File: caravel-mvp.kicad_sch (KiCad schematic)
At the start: 46 parts, among them J2 Conn_01x02, J3 Conn_02x04_Odd_Even, J4 Conn_01x06, J6 Conn_02x18_Odd_Even, J6 USB_C_Receptacle_USB2.0, J9 613012243121, SW3 B3U-1000P, U1 Caravel_QFN, U1 W25Q32JVSS, X1 10MHz

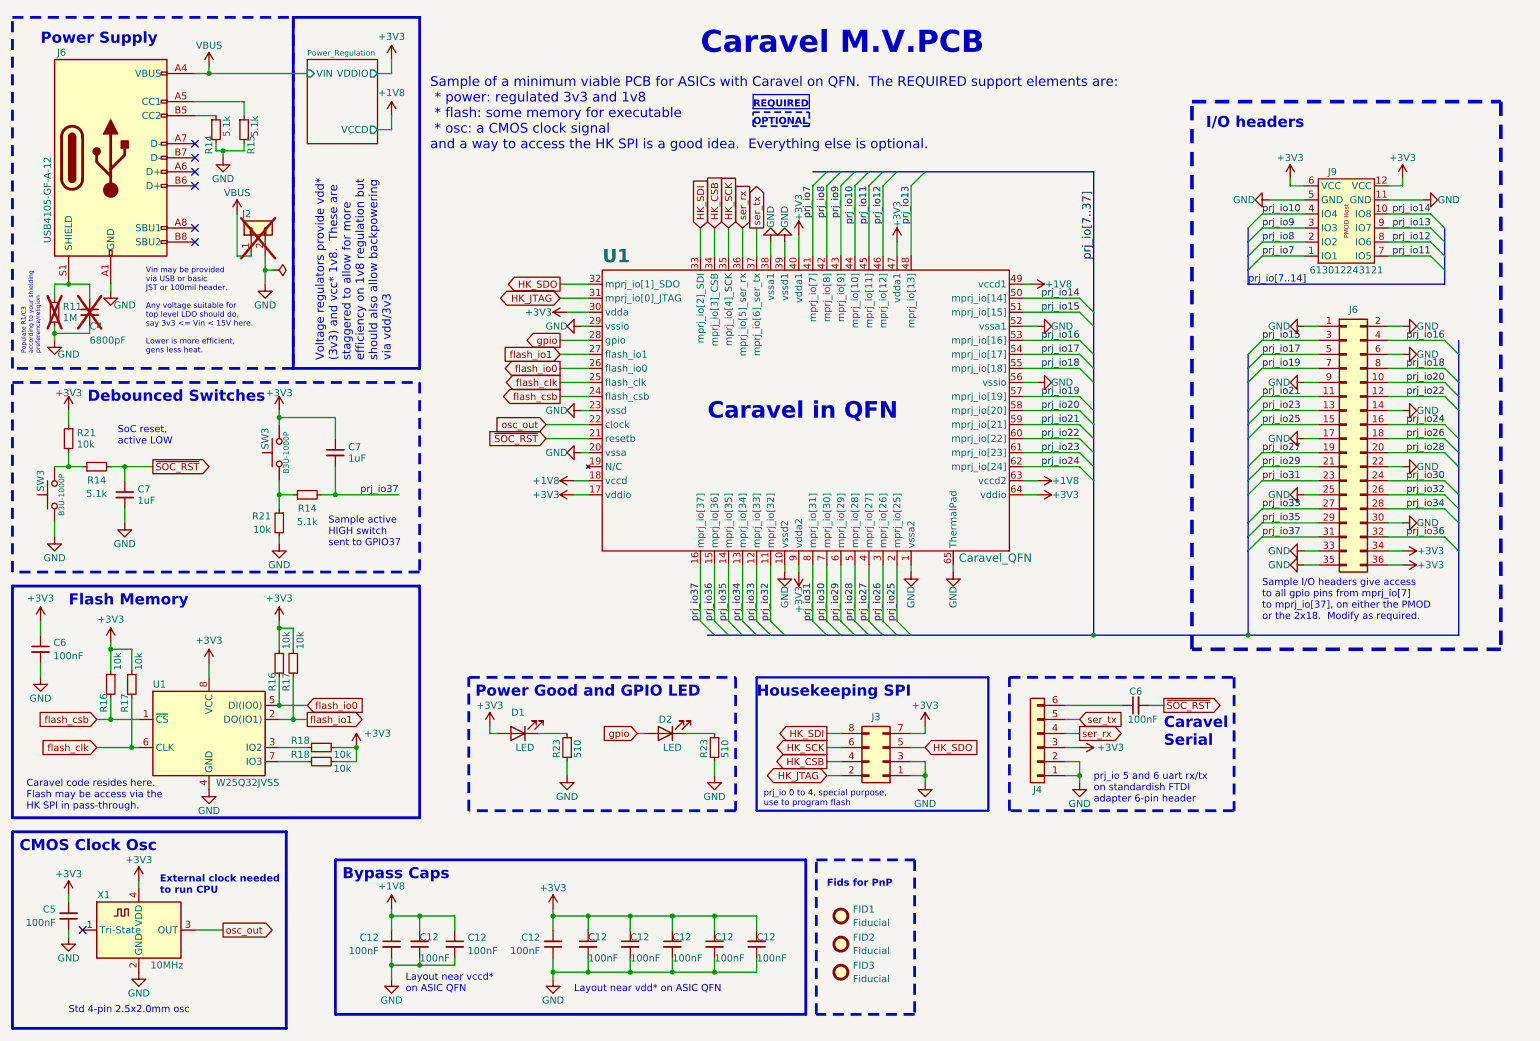
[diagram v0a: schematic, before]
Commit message: TinyTapeout 1-2-3 version
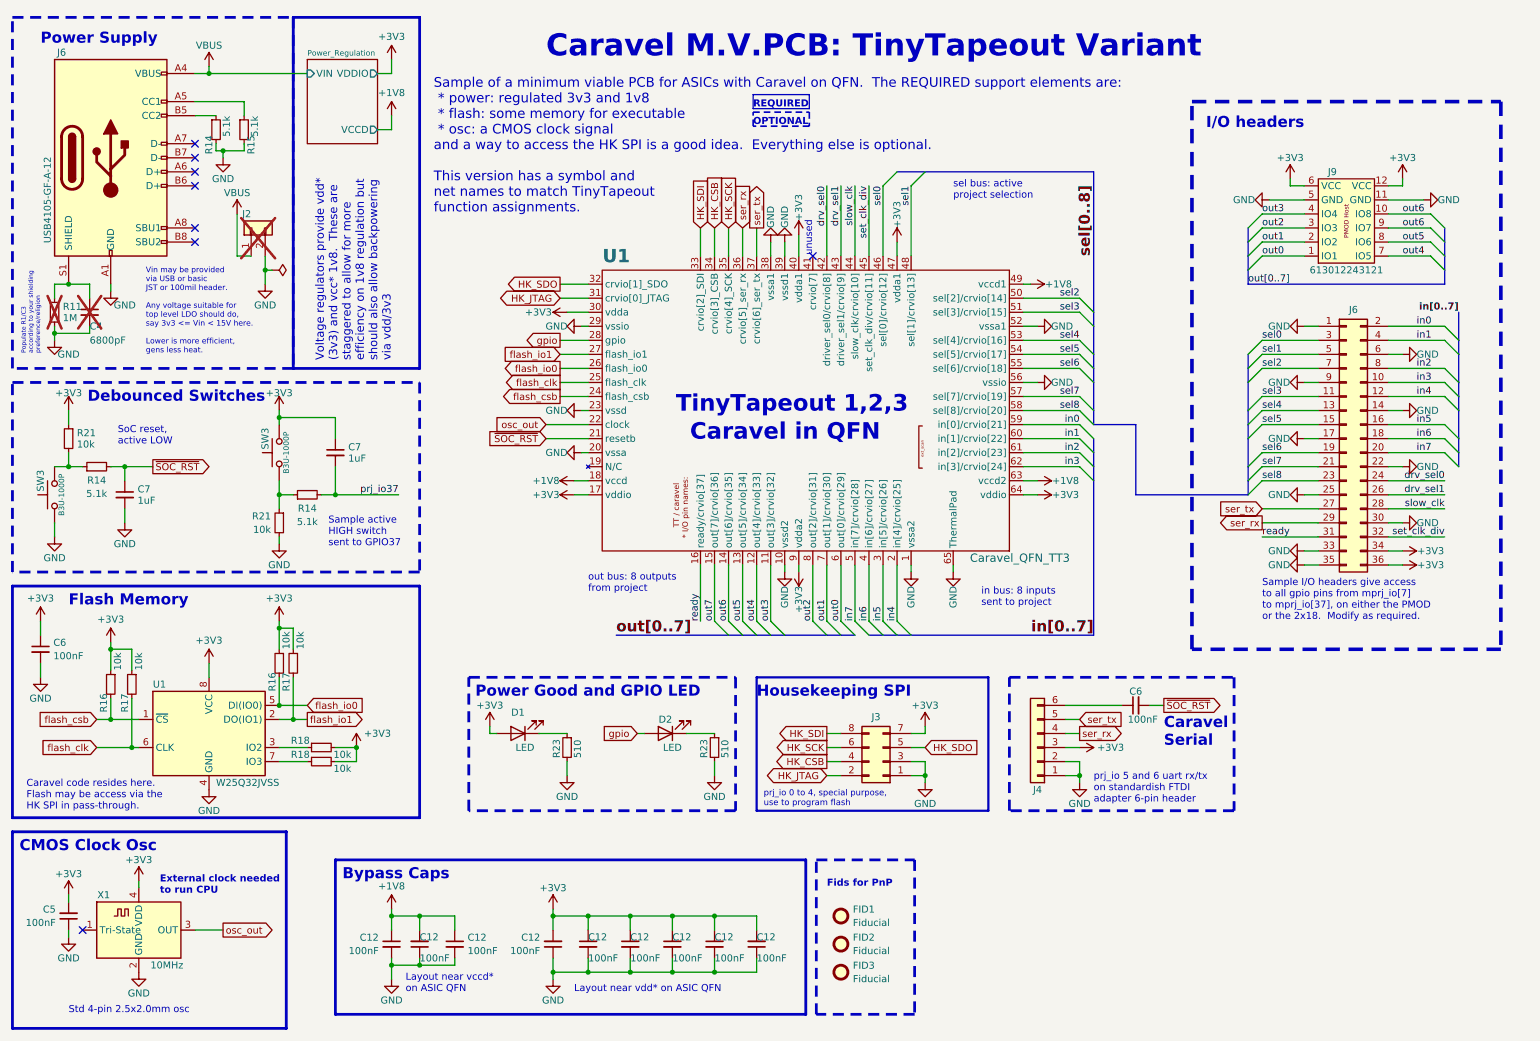
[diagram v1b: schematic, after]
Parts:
- U1: value Caravel_QFN -> Caravel_QFN_TT3; symbol TinyTapeout:Caravel_QFN -> TinyTapeout:Caravel_QFN_TT3
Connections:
- net GND: no longer J6.2 (Pin_2)
- net prj_io37: no longer J6.31 (Pin_31), U1.16 (mprj_io[37])
- net ser_rx: now also J6.29 (Pin_29)
- net ser_tx: now also J6.27 (Pin_27)
- net prj_io10 renamed out3
- net out3: now also U1.11 (out[3]/crvio[32]); no longer U1.44 (mprj_io[10])
- net prj_io11 renamed out4
- net out4: now also U1.12 (out[4]/crvio[33]); no longer U1.45 (mprj_io[11])
- net prj_io12 renamed out5
- net out5: now also U1.13 (out[5]/crvio[34]); no longer U1.46 (mprj_io[12])
- net prj_io13 renamed out6
- net out6: now also J9.10 (IO8), U1.14 (out[6]/crvio[35]); no longer U1.48 (mprj_io[13])
- net prj_io14 renamed sel2
- net sel2: now also J6.7 (Pin_7); no longer J9.10 (IO8)
- net prj_io15 renamed sel0
- net sel0: now also U1.46 (sel[0]/crvio[12]); no longer U1.51 (mprj_io[15])
- net prj_io16 renamed in1
- net in1: now also U1.60 (in[1]/crvio[22]); no longer U1.53 (mprj_io[16])
- net prj_io17 renamed sel1
- net sel1: now also U1.48 (sel[1]/crvio[13]); no longer U1.54 (mprj_io[17])
- net prj_io18 renamed in2
- net in2: now also U1.61 (in[2]/crvio[23]); no longer U1.55 (mprj_io[18])
- net prj_io19 renamed sel7
- net sel7: now also J6.21 (Pin_21); no longer J6.7 (Pin_7)
- net prj_io20 renamed in3
- net in3: now also U1.62 (in[3]/crvio[24]); no longer U1.58 (mprj_io[20])
- net prj_io21 renamed in0
- net in0: now also J6.2 (Pin_2); no longer J6.11 (Pin_11)
- net prj_io22 renamed in4
- net in4: now also U1.2 (in[4]/crvio[25]); no longer U1.60 (mprj_io[22])
- net prj_io23 renamed sel4
- net sel4: now also U1.53 (sel[4]/crvio[16]); no longer U1.61 (mprj_io[23])
- net prj_io24 renamed in5
- net in5: now also U1.3 (in[5]/crvio[26]); no longer U1.62 (mprj_io[24])
- net prj_io25 renamed sel5
- net sel5: now also U1.54 (sel[5]/crvio[17]); no longer U1.2 (mprj_io[25])
- net prj_io26 renamed in6
- net in6: now also U1.4 (in[6]/crvio[27]); no longer U1.3 (mprj_io[26])
- net prj_io27 renamed sel6
- net sel6: now also U1.55 (sel[6]/crvio[18]); no longer U1.4 (mprj_io[27])
- net prj_io28 renamed in7
- net prj_io29 renamed out0
- net out0: now also J9.1 (IO1); no longer J6.21 (Pin_21)
- net prj_io30 renamed drv_sel0
- net drv_sel0: now also U1.42 (driver_sel0/crvio[8]); no longer U1.7 (mprj_io[30])
- net prj_io31 renamed out2
- net out2: now also J9.3 (IO3); no longer J6.23 (Pin_23)
- net prj_io32 renamed drv_sel1
- net drv_sel1: now also U1.43 (driver_sel1/crvio[9]); no longer U1.11 (mprj_io[32])
- removed net prj_io33: J6.27 (Pin_27), U1.12 (mprj_io[33])
- net prj_io34 renamed slow_clk
- net slow_clk: now also U1.44 (slow_clk/crvio[10]); no longer U1.13 (mprj_io[34])
- removed net prj_io35: J6.29 (Pin_29), U1.14 (mprj_io[35])
- net prj_io36 renamed out7
- net out7: no longer J6.32 (Pin_32)
- net prj_io7: no longer names the net of U1.41 (crvio[7])
- net prj_io7: no longer J9.1 (IO1)
- net prj_io8 renamed out1
- net out1: now also U1.7 (out[1]/crvio[30]); no longer U1.42 (mprj_io[8])
- removed net prj_io9: J9.3 (IO3), U1.43 (mprj_io[9])
- new net ready: J6.31 (Pin_31), U1.16 (ready/crvio[37])
- new net sel3: J6.11 (Pin_11), U1.51 (sel[3]/crvio[15])
- new net sel8: J6.23 (Pin_23), U1.58 (sel[8]/crvio[20])
- new net set_clk_div: J6.32 (Pin_32), U1.45 (set_clk_div/crvio[11])
- no-connect marks 7 -> 8
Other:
- note added: "Caravel M.V.PCB: TinyTapeout Variant"
- note added: "Sample of a minimum viable PCB for ASICs with Caravel on QFN. The REQUIRED support elements are: * power: regulated 3v3 and 1v8 * flash: some memory for executable * osc: a CMOS clock signal and a way to access the HK SPI is a good idea. Everything else is optional. This version has a symbol and net names to match TinyTapeout function assignments."
- note added: "TinyTapeout 1,2,3"
- note added: "in bus: 8 inputs sent to project"
- note added: "out bus: 8 outputs from project"
- note added: "sel bus: active project selection"
- note added: "unused"
- note removed: "Caravel M.V.PCB"
- note removed: "Sample of a minimum viable PCB for ASICs with Caravel on QFN. The REQUIRED support elements are: * power: regulated 3v3 and 1v8 * flash: some memory for executable * osc: a CMOS clock signal and a way to access the HK SPI is a good idea. Everything else is optional."
- title: Caravel Minimum Viable PCB Example -> Caravel Minimum Viable PCB Example: TinyTapeout Version

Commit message: TinyTapeout Stand-alone (no CPU) circuit and info
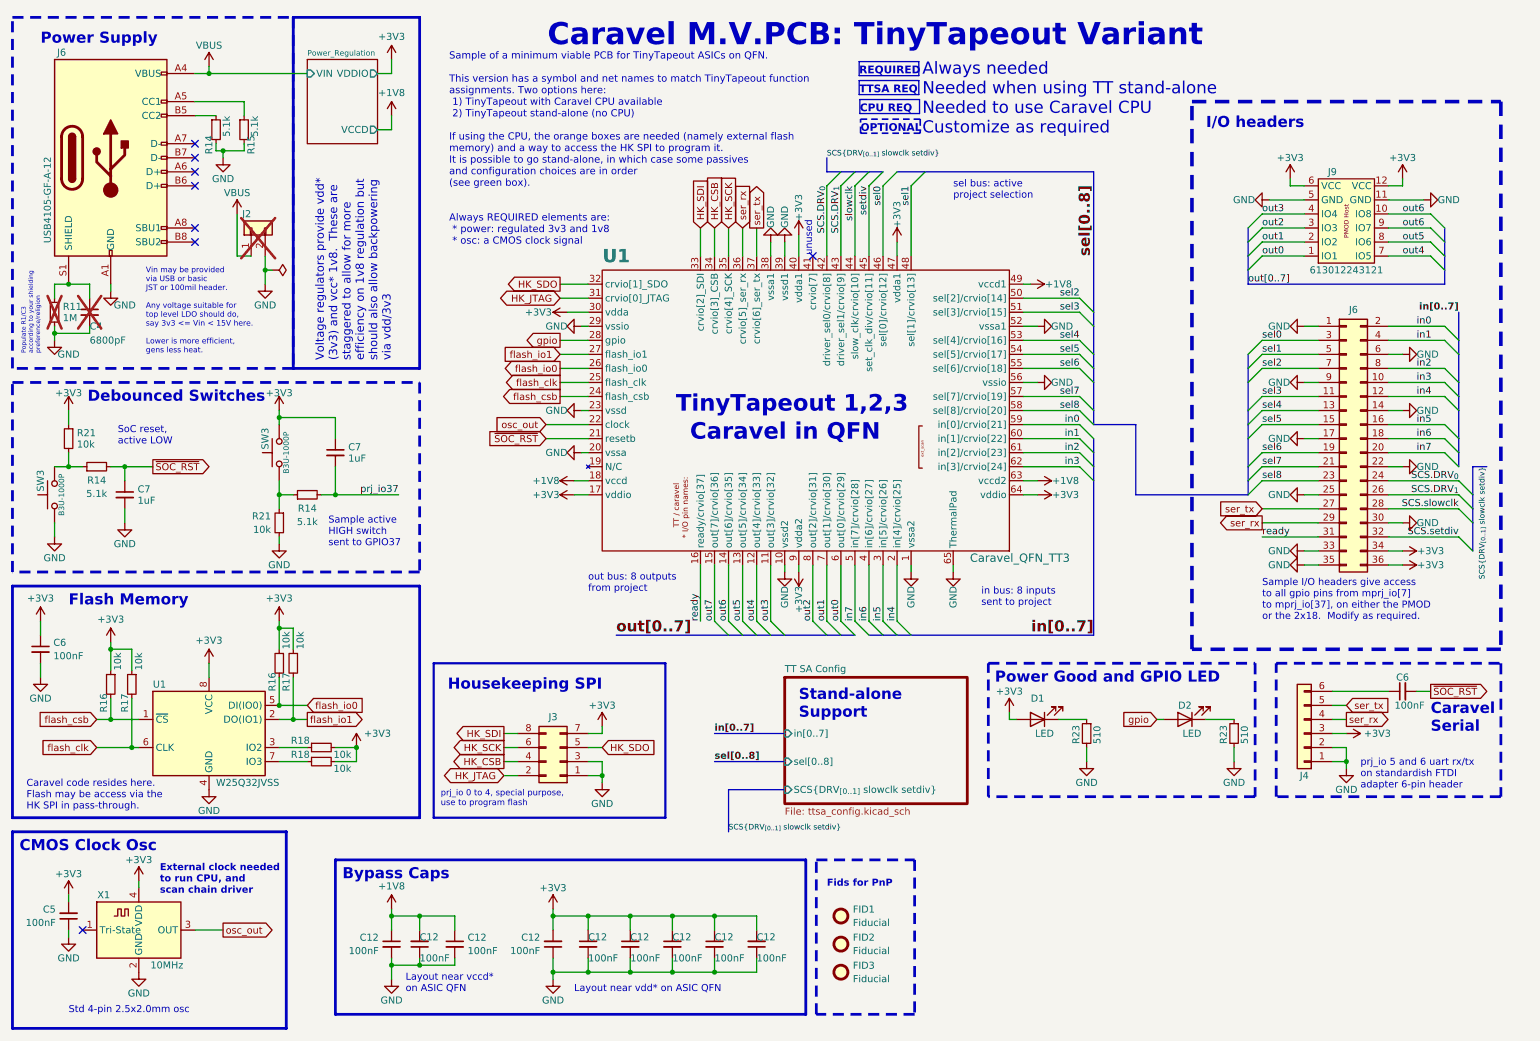
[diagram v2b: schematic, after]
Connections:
- net drv_sel0 renamed SCS.DRV_{0}
- net drv_sel1 renamed SCS.DRV_{1}
- net set_clk_div renamed SCS.setdiv
- net SCS.setdiv: no longer U1.45 (set_clk_div/crvio[11])
- net slow_clk renamed SCS.slowclk
- net SCS.slowclk: no longer U1.44 (slow_clk/crvio[10])
- new net setdiv: U1.45 (set_clk_div/crvio[11])
- new net slowclk: U1.44 (slow_clk/crvio[10])
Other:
- added sheet TT SA Config (ttsa_config.kicad_sch)
- note added: "Always needed Needed when using TT stand-alone Needed to use Caravel CPU Customize as required"
- note added: "CPU REQ"
- note added: "External clock needed to run CPU, and scan chain driver"
- note added: "Sample of a minimum viable PCB for TinyTapeout ASICs on QFN. This version has a symbol and net names to match TinyTapeout function assignments. Two options here: 1) TinyTapeout with Caravel CPU available 2) TinyTapeout stand-alone (no CPU) If using the CPU, the orange boxes are needed (namely external flash memory) and a way to access the HK SPI to program it. It is possible to go stand-alone, in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"
- note added: "Stand-alone Support"
- note added: "TTSA REQ"
- note removed: "External clock needed to run CPU"
- note removed: "Sample of a minimum viable PCB for ASICs with Caravel on QFN. The REQUIRED support elements are: * power: regulated 3v3 and 1v8 * flash: some memory for executable * osc: a CMOS clock signal and a way to access the HK SPI is a good idea. Everything else is optional. This version has a symbol and net names to match TinyTapeout function assignments."
- moved on the sheet: C6, D1, D2, J3, J4, R23

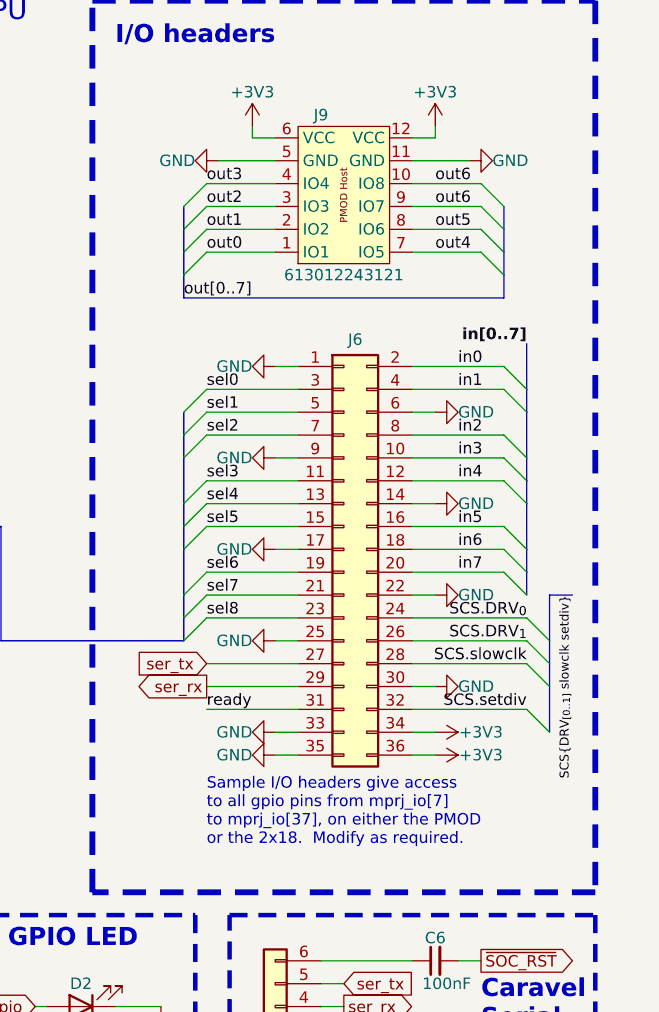
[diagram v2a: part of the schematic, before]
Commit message: Friendlier sort of scan drive bits, and more doc
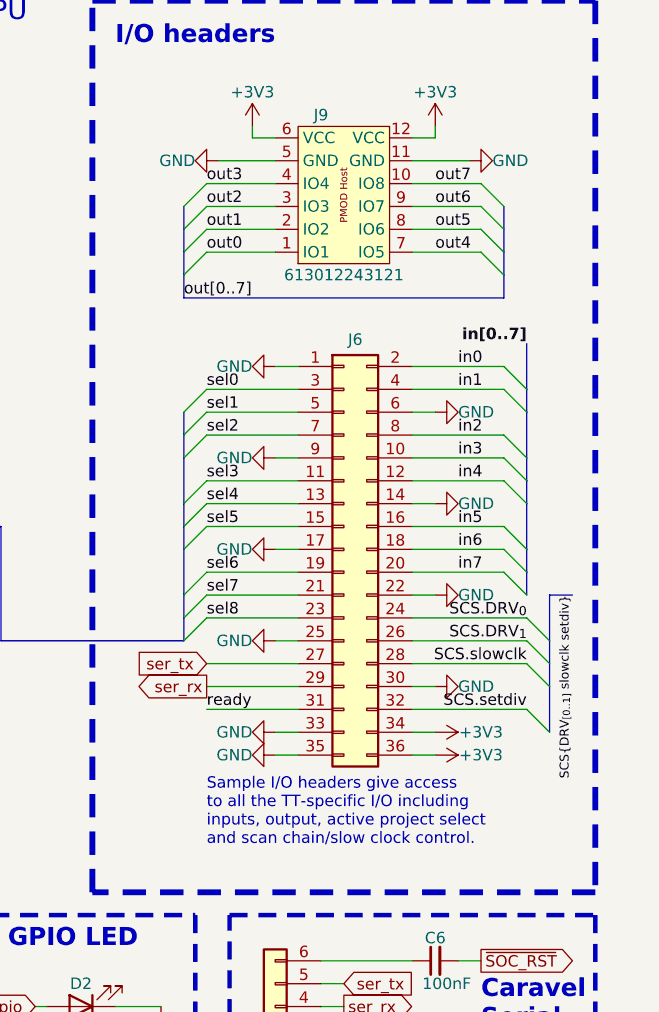
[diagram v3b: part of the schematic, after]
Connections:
- net out6: no longer J9.10 (IO8)
- net out7: now also J9.10 (IO8)
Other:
- note added: "Sample I/O headers give access to all the TT-specific I/O including inputs, output, active project select and scan chain/slow clock control."
- note removed: "Sample I/O headers give access to all gpio pins from mprj_io[7] to mprj_io[37], on either the PMOD or the 2x18. Modify as required."
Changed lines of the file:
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@@
     (effects (font (size 1.27 1.27)) (justify left bottom))
   )
-  (text "Sample I/O headers give access\nto all gpio pins from mprj_io[7] \nto mprj_io[37], on either the PMOD\nor the 2x18.  Modify as required."
+  (text "Sample I/O headers give access\nto all the TT-specific I/O including\ninputs, output, active project select\nand scan chain/slow clock control.\n"
     (at 238.76 121.92 0)
     (effects (font (size 1.27 1.27)) (justify left bottom))
@@
     (effects (font (size 1.27 1.27)) (justify left bottom))
   )
-  (label "out6" (at 264.16 48.26 0) (fields_autoplaced)
+  (label "out7" (at 264.16 48.26 0) (fields_autoplaced)
     (effects (font (size 1.27 1.27)) (justify left bottom))
   )
